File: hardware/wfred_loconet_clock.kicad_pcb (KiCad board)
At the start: 2 copper layers, 124 x 35 mm, 65 parts, among them IC201 ATMEGA328P-A, J301 Molex 95501-6669, K301 TERMINATION, K401 UART_ESP, K402 UART_AVR, P201 ISP, P401 ESP_BOOTLOAD, P501 CLOCK, Q301 BC817-40, Q302 BC817-40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

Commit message: Fixed PCB after untangling
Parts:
- removed C201, C202, C203, C204, C303: 100n, Capacitors_SMD:C_0805_HandSoldering
- removed C205, C206: 22p, Capacitors_SMD:C_0805_HandSoldering
- removed C301: 1n, Capacitors_SMD:C_0805_HandSoldering
- removed C302: 47p, Capacitors_SMD:C_0805_HandSoldering
- removed C304, C305: 22u, Capacitors_SMD:C_0805_HandSoldering
- removed D301, D302, D303: BAR43, TO_SOT_Packages_SMD:SOT-23_Handsoldering
- removed IC201: ATMEGA328P-A, Housings_QFP:TQFP-32_7x7mm_Pitch0.8mm
- removed J301: Molex 95501-6669, myFootprints:Molex_95501-6669
- removed K301: TERMINATION, Pin_Headers:Pin_Header_Straight_1x03_Pitch2.54mm
- removed K402: UART_AVR, Pin_Headers:Pin_Header_Straight_1x03_Pitch2.54mm
- removed P201: ISP, Pin_Headers:Pin_Header_Straight_2x03_Pitch2.54mm
- removed Q301, Q302, Q303: BC817-40, TO_SOT_Packages_SMD:SOT-23_Handsoldering
- removed R201: 10k, Capacitors_SMD:C_0805_HandSoldering
- removed R301: 4k7, Capacitors_SMD:C_0805_HandSoldering
- removed R302, R304, R310: 47k, Capacitors_SMD:C_0805_HandSoldering
- removed R303: 47R, Capacitors_SMD:C_0805_HandSoldering
- removed R305: 2k2, Capacitors_SMD:C_0805_HandSoldering
- removed R306: 82k, Capacitors_SMD:C_0805_HandSoldering
- removed R307, R308: 12R, Capacitors_SMD:C_0805_HandSoldering
- removed R309, R401, R402: 100k, Capacitors_SMD:C_0805_HandSoldering
- removed U301: TC1240, TO_SOT_Packages_SMD:SOT-23-6_Handsoldering
- removed X201: myCRYSTAL, Crystals:Crystal_SMD_TXC_7M-4pin_3.2x2.5mm_HandSoldering
- moved K401 1.54 mm to (76.5, 107.0)
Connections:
- U401 pad 1: VCC -> (no net)
- U401 pad 13: LOCO2 -> CLOCK2
- U401 pad 14: LOCO1 -> CLOCK1
- U401 pad 2: Net-(R401-Pad2) -> (no net)
- U401 pad 4: CLOCK1 -> LOCO1
- U401 pad 5: CLOCK2 -> LOCO2
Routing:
- net GND: track 381.9 -> 56.0 mm, vias 5 -> 0
- net VCC: track 244.7 -> 16.0 mm
- net CLOCK1: track 90.1 -> 0.00 mm, vias 1 -> 0
- net CLOCK2: track 82.9 -> 0.00 mm, vias 1 -> 0
- net THIS_TXD: track 81.0 -> 0.00 mm, vias 1 -> 0
- net THIS_RXD: track 76.3 -> 0.00 mm, vias 1 -> 0
- net Net-(D501-Pad2): track 70.5 -> 0.00 mm
- net MISO: track 68.0 -> 0.00 mm, vias 3 -> 0
- net LOCO2: track 65.1 -> 0.00 mm, vias 1 -> 0
- net LOCO1: track 64.4 -> 0.00 mm, vias 1 -> 0
- net +5V: track 63.1 -> 0.00 mm, vias 1 -> 0
- net ESTOP: track 62.2 -> 0.00 mm, vias 3 -> 0
- net SCK: track 59.9 -> 0.00 mm, vias 3 -> 0
- net +BATT: track 57.1 -> 0.00 mm, vias 2 -> 0
- net RESET: track 51.2 -> 0.00 mm, vias 1 -> 0
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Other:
- board text added: "WiFi-Clock rev0.3 Heiko Rosemann"
- board text removed: "wfred rev0.2 Heiko Rosemann"

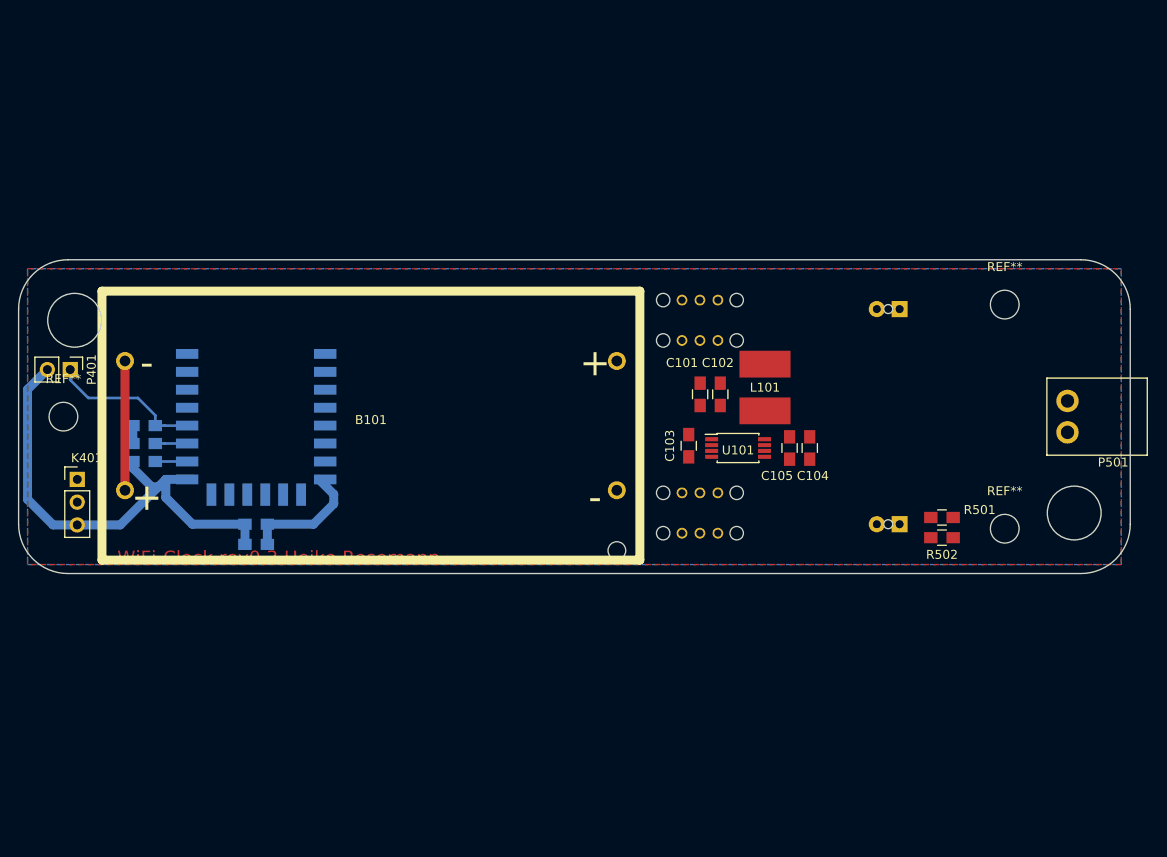
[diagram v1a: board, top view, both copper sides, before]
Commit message: Change clock schematic and PCB
- Remove slide switches, replace with single push button
- Add status LED
- Re-add battery measurement connection

- Change PCB form factor to fit NewAgeEnclosures Compact AA housing
- Re-layout PCB
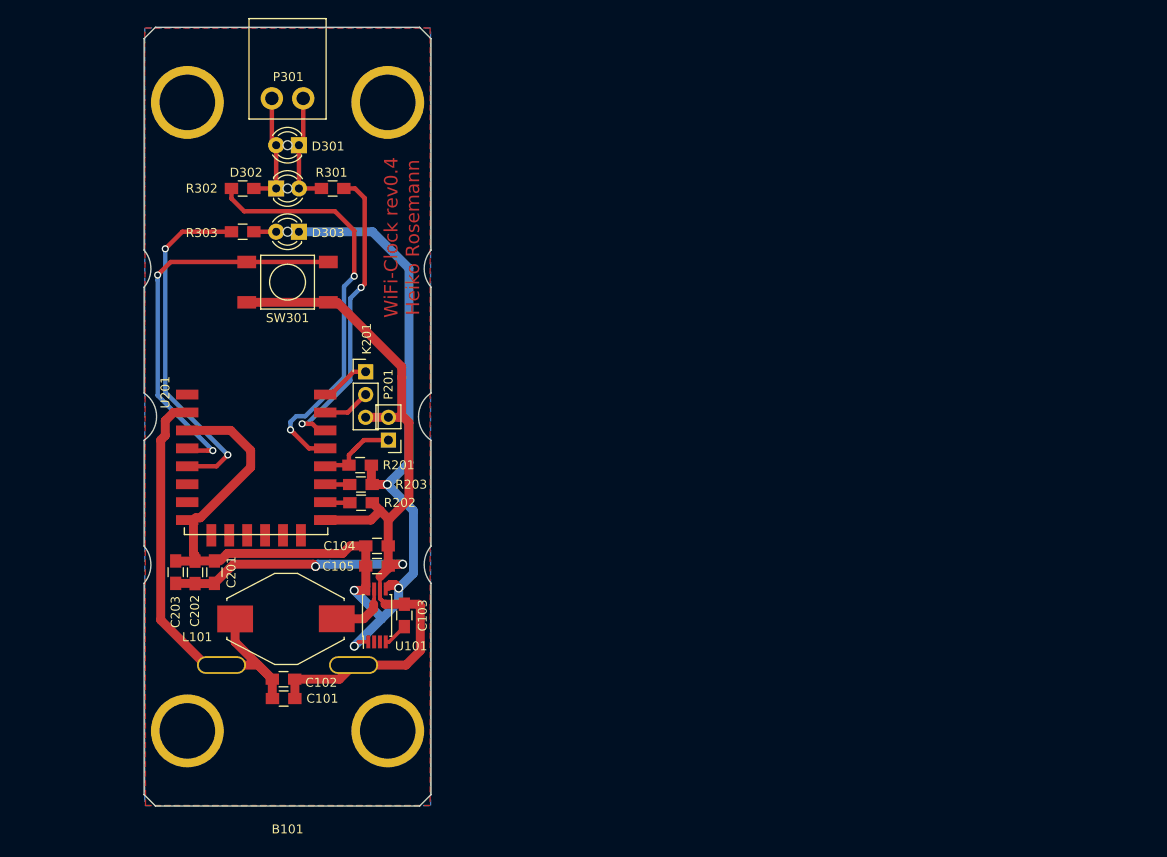
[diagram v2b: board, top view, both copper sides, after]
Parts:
- removed C401: 100n, Capacitors_SMD:C_0805_HandSoldering
- removed C402: 22u, Capacitors_SMD:C_0805_HandSoldering
- removed D501, D502: red, myFootprints:LED_D3.0mm
- removed K401: UART_ESP, Pin_Headers:Pin_Header_Straight_1x03_Pitch2.54mm
- removed P401: ESP_BOOTLOAD, Pin_Headers:Pin_Header_Straight_1x02_Pitch2.54mm
- removed P501: CLOCK, myFootprints:AKL183-02
- removed R403, R404, R405: 10k, Capacitors_SMD:C_0805_HandSoldering
- removed R501, R502: 220, Capacitors_SMD:C_0805_HandSoldering
- removed REF** (x3): MountingHole_3.2mm_M3, Mounting_Holes:MountingHole_3.2mm_M3
- removed SW501, SW502, SW503, SW504: SWITCH_INV, myFootprints:OS102011MS2Q
- removed U401: ESP-12E, ESP8266:ESP-12E_SMD
- added C201: 100n, Capacitors_SMD:C_0805_HandSoldering, F.Cu at (91.8, 117.3)
- added C202: 22u, Capacitors_SMD:C_0805_HandSoldering, F.Cu at (89.7, 117.4)
- added C203: 100u, Capacitors_SMD:C_0805_HandSoldering, F.Cu at (87.5, 117.3)
- added D301: red, myFootprints:LED_D3.0mm, F.Cu at (101.3, 69.7)
- added D302: red, myFootprints:LED_D3.0mm, F.Cu at (98.7, 74.5)
- added D303: red, myFootprints:LED_D3.0mm, F.Cu at (101.3, 79.4)
- added K201: UART_ESP, Pin_Headers:Pin_Header_Straight_1x03_Pitch2.54mm, F.Cu at (108.7, 95.0)
- added P201: ESP_BOOTLOAD, Pin_Headers:Pin_Header_Straight_1x02_Pitch2.54mm, F.Cu at (111.3, 102.6)
- added P301: CLOCK, myFootprints:AKL183-02, F.Cu at (101.8, 64.5)
- added R201: 10k, Capacitors_SMD:C_0805_HandSoldering, F.Cu at (108.1, 105.4)
- added R202: 10k, Capacitors_SMD:C_0805_HandSoldering, F.Cu at (108.2, 109.6)
- added R203: 10k, Capacitors_SMD:C_0805_HandSoldering, F.Cu at (108.2, 107.6)
- added R301: 220, Capacitors_SMD:C_0805_HandSoldering, F.Cu at (105.0, 74.5)
- added R302: 220, Capacitors_SMD:C_0805_HandSoldering, F.Cu at (95.0, 74.5)
- added R303: 330, Capacitors_SMD:C_0805_HandSoldering, F.Cu at (95.0, 79.4)
- added SW301: SW_PUSH, myFootprints:Taster_9319, F.Cu at (100.0, 85.0)
- added U201: ESP-12E, ESP8266:ESP-12E_SMD, F.Cu at (89.5, 97.5)
- B101: value BATT_HOLDER -> BATT_HOLDER_2; footprint myFootprints:KEYSTONE1013 -> myFootprints:NEW_AGE_COMPACT_AA_PCBEdges
- L101: footprint myFootprints:L_2424_HandSoldering -> Inductors_SMD:L_Fastron_PISN_Handsoldering
- moved L101 59.3 mm to (99.8, 122.6), turned to 180 degrees
- moved C102 58.2 mm to (99.5, 129.3), turned to 0 degrees
- moved C101 57.5 mm to (99.6, 131.4), turned to 0 degrees
- moved C104 49.5 mm to (110.0, 114.4), turned to 0 degrees
- moved C105 47.9 mm to (110.0, 116.7), turned to 0 degrees
- moved U101 44.4 mm to (110.0, 122.2), turned to 90 degrees
- moved C103 36.9 mm to (113.0, 122.2)
- moved B101 9.35 mm to (100.0, 100.0)
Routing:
- net VCC: track 16.0 -> 139.7 mm, vias 0 -> 4
- net GND: track 56.0 -> 119.2 mm, vias 0 -> 2
- net +BATT: track 0.00 -> 51.7 mm
- net CLOCK2: track 0.00 -> 46.1 mm, vias 0 -> 2
- net KEY: track 0.00 -> 44.0 mm, vias 0 -> 2
- net STATUS_LED: track 0.00 -> 38.4 mm, vias 0 -> 2
- net CLOCK1: track 0.00 -> 33.4 mm, vias 0 -> 2
- net Net-(P401-Pad1): track 17.7 -> 0.00 mm
- net Net-(B101-PadMI1): track 14.4 -> 0.00 mm
- net Net-(D301-Pad2): track 0.00 -> 12.8 mm
- net Net-(D301-Pad1): track 0.00 -> 12.8 mm
- net Net-(P201-Pad1): track 0.00 -> 10.3 mm
- net Net-(L101-Pad2): track 0.00 -> 7.34 mm
- net Net-(K201-Pad1): track 0.00 -> 6.45 mm
- net Net-(K201-Pad2): track 0.00 -> 6.04 mm
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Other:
- board size 124 x 35 mm -> 32 x 86.9 mm
- net class Default: trace_width 0.3 -> 0.5
- board text added: "WiFi-Clock rev0.4 Heiko Rosemann"
- board text removed: "WiFi-Clock rev0.3 Heiko Rosemann"

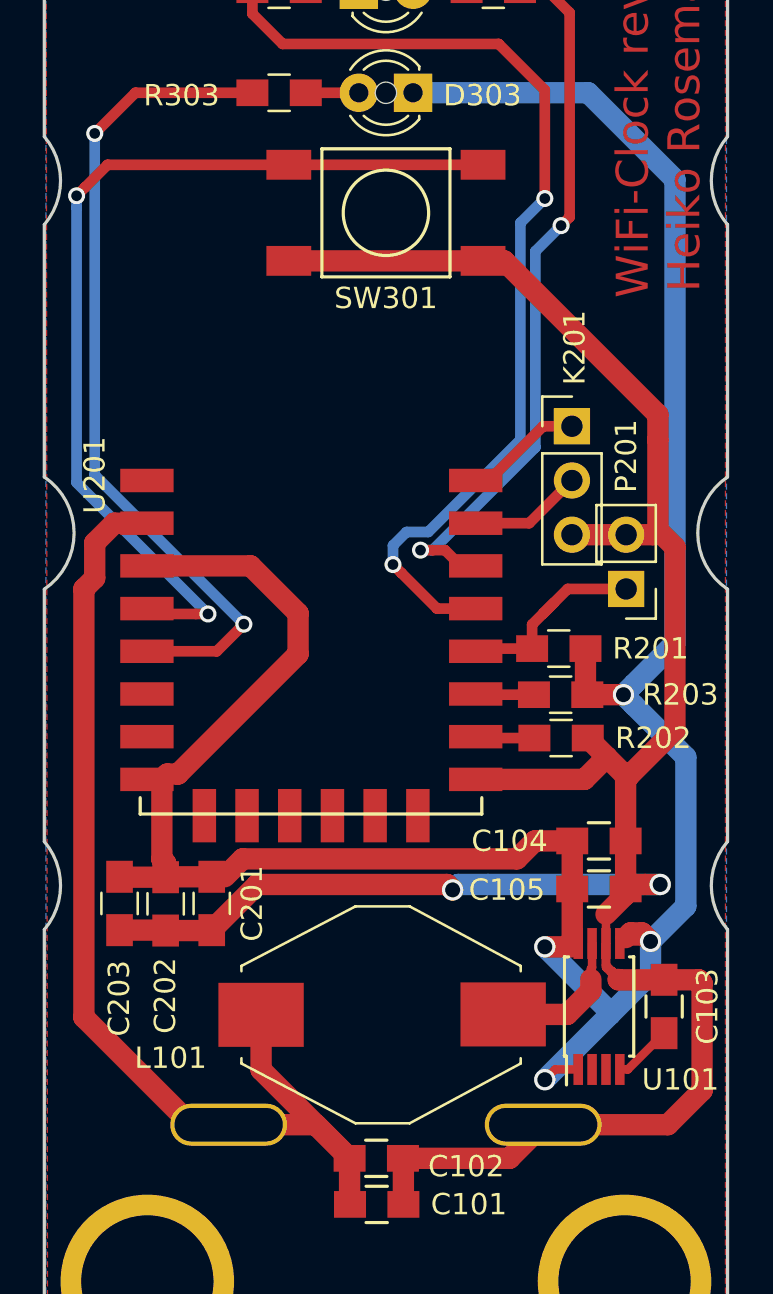
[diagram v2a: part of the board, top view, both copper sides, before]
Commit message: Changed PCB and code to closer match first PCB
- Add battery measurement resistors
- Move key, status LED and clock I/O-pins around to match first PCB
  (except for CLOCK1 which is on low power pin in first version)
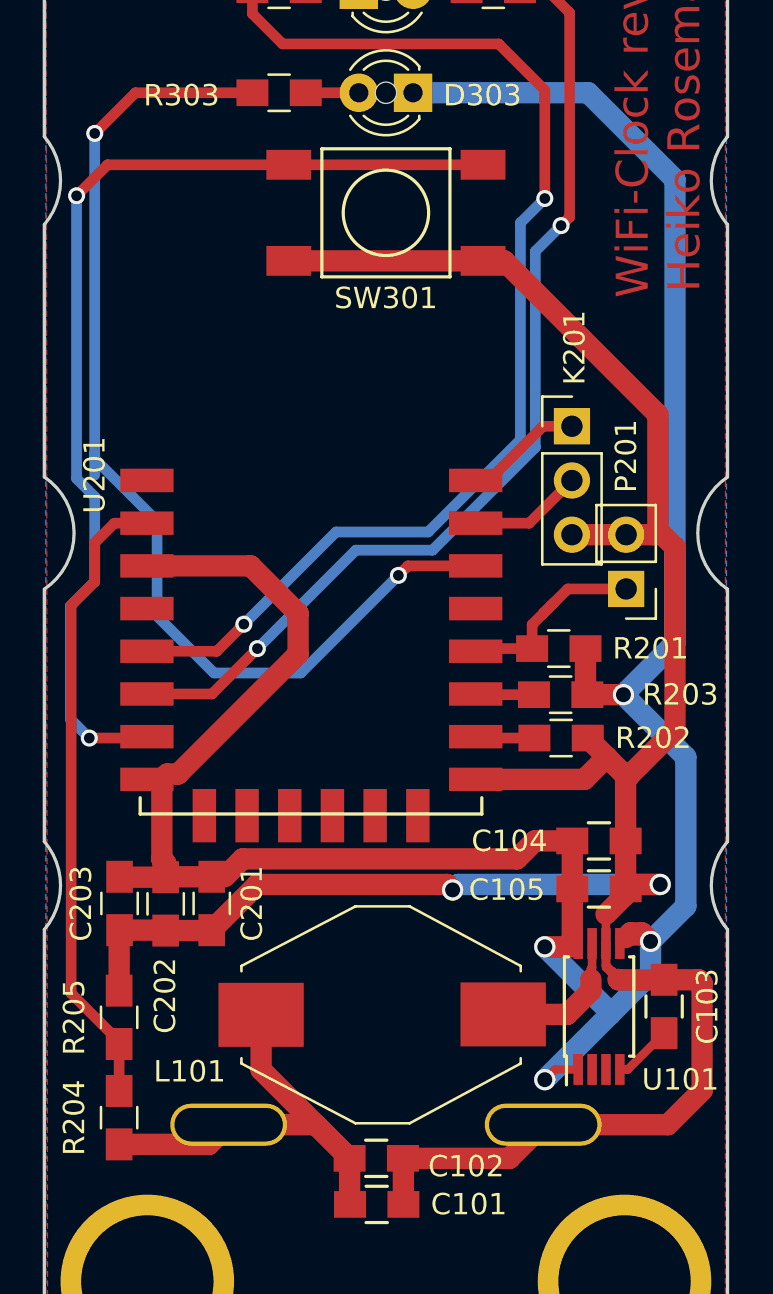
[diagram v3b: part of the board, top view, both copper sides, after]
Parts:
- added R204: 100k, Capacitors_SMD:C_0805_HandSoldering, F.Cu at (87.5, 127.4)
- added R205: 47k, Capacitors_SMD:C_0805_HandSoldering, F.Cu at (87.5, 122.7)
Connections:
- U201 pad 13: CLOCK2 -> (no net)
- U201 pad 14: CLOCK1 -> STATUS_LED
- U201 pad 2: +BATT -> Net-(R204-Pad2)
- U201 pad 4: KEY -> (no net)
- U201 pad 5: STATUS_LED -> CLOCK2
- U201 pad 6: (no net) -> CLOCK1
- U201 pad 7: (no net) -> KEY
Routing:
- net Net-(R204-Pad2): track 0.00 -> 30.6 mm
- net +BATT: track 51.7 -> 24.2 mm
- net CLOCK1: track 33.4 -> 46.1 mm
- net STATUS_LED: track 38.4 -> 50.4 mm
- net CLOCK2: track 46.1 -> 54.1 mm
- net KEY: track 44.0 -> 49.7 mm
- net GND: track 119.2 -> 122.1 mm

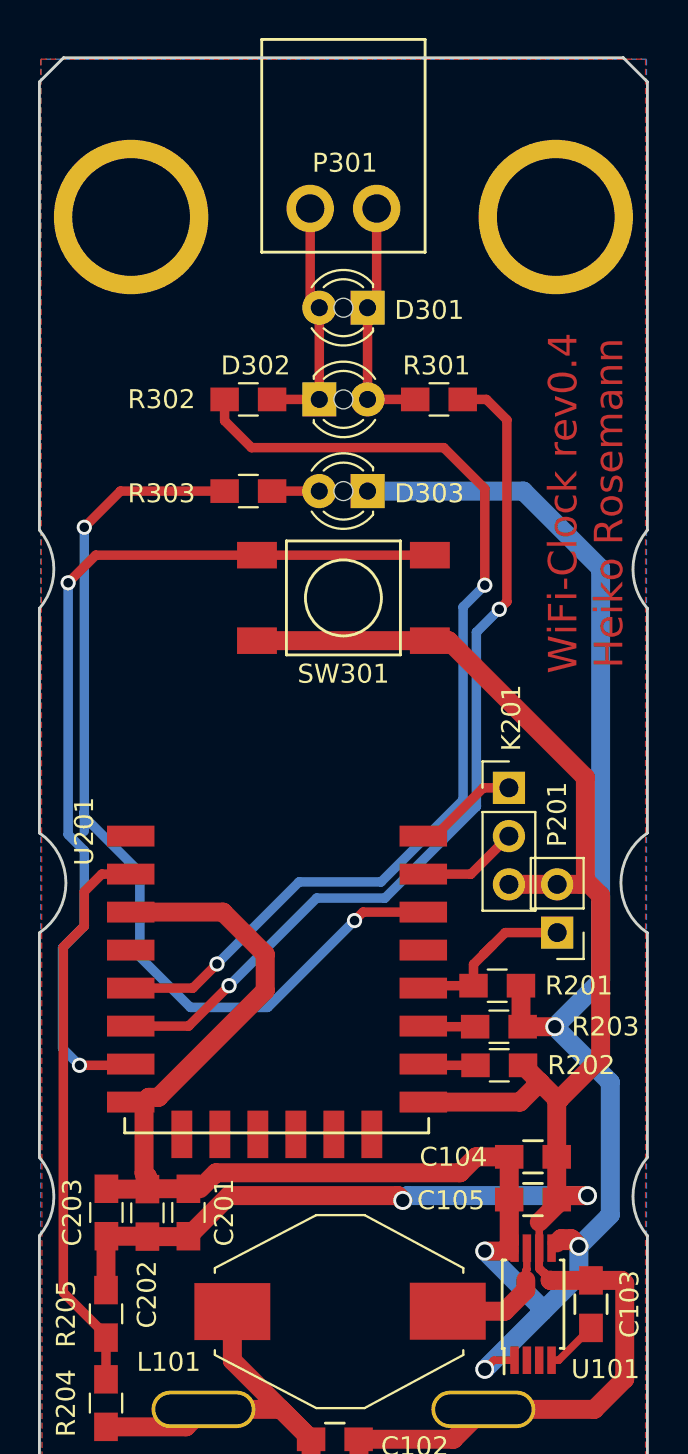
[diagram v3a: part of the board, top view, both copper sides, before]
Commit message: Added more keys to the PCB for adjusting the time
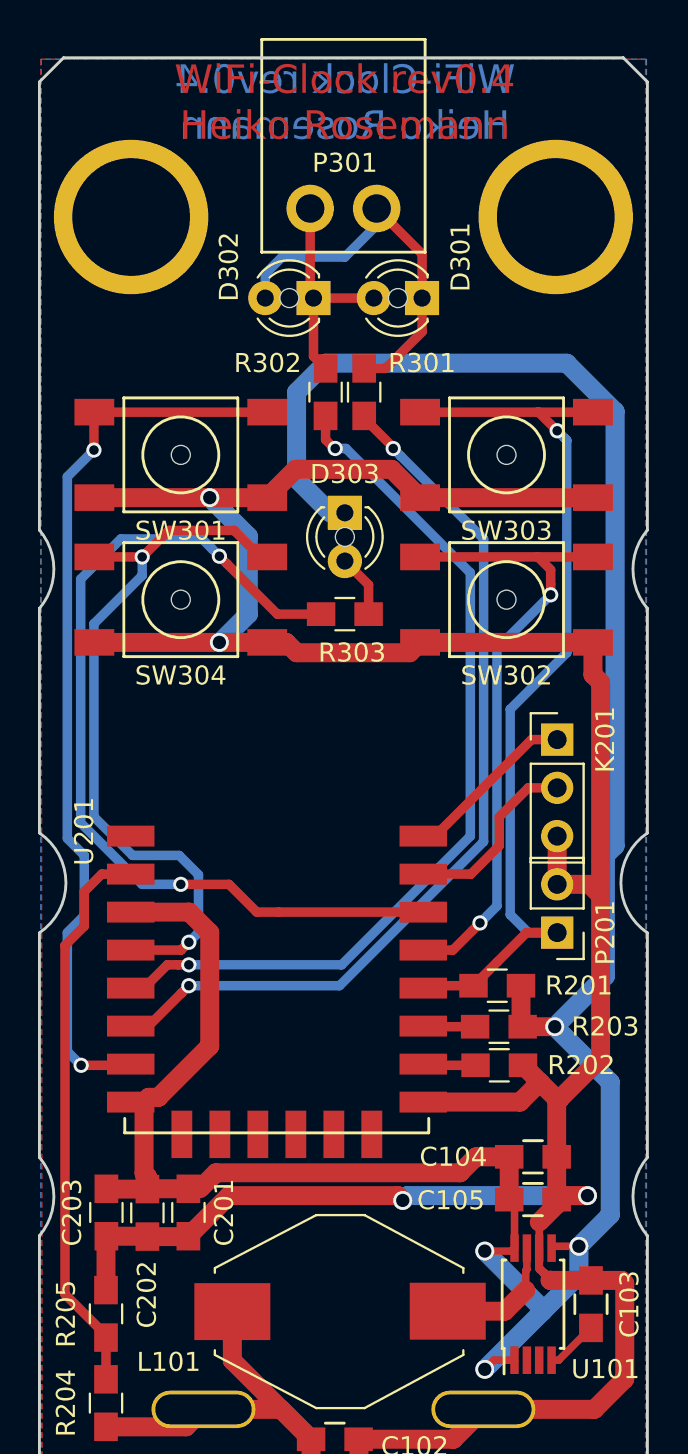
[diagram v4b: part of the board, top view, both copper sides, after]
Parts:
- added SW302: SW_PUSH, myFootprints:Taster_9319, F.Cu at (108.6, 85.1)
- added SW303: SW_PUSH, myFootprints:Taster_9319, F.Cu at (108.6, 77.5)
- added SW304: SW_PUSH, myFootprints:Taster_9319, F.Cu at (91.4, 85.1)
- moved SW301 11.4 mm to (91.4, 77.5)
- moved R303 8.23 mm to (100.1, 85.9)
- moved D302 5.34 mm to (98.4, 69.2), turned to 180 degrees
- moved R302 4.08 mm to (99.1, 74.2), turned to 270 degrees
- moved R301 3.96 mm to (101.1, 74.2), turned to 270 degrees
- moved K201 3.59 mm to (111.3, 92.5)
- moved D301 2.91 mm to (104.1, 69.2)
- moved D303 1.65 mm to (100.1, 80.5), turned to 270 degrees
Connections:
- net Net-(P201-Pad1) renamed KEY_MINUTE
- SW301 pad 2: KEY -> KEY_CONF
- U201 pad 13: (no net) -> KEY_HOUR
- U201 pad 4: (no net) -> KEY
- U201 pad 7: KEY -> KEY_CONF
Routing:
- net GND: track 122.1 -> 173.0 mm, vias 2 -> 4
- net KEY_CONF: track 0.00 -> 48.4 mm, vias 0 -> 2
- net KEY_MINUTE: track 10.3 -> 49.3 mm, vias 0 -> 1
- net KEY_HOUR: track 0.00 -> 34.5 mm, vias 0 -> 2
- net VCC: track 139.7 -> 152.1 mm
- net KEY: track 49.7 -> 38.1 mm
- net CLOCK2: track 54.1 -> 46.1 mm
- net Net-(D301-Pad1): track 12.8 -> 20.4 mm
- net Net-(K201-Pad2): track 6.04 -> 10.5 mm
- net Net-(K201-Pad1): track 6.45 -> 10.0 mm
- net STATUS_LED: track 50.4 -> 47.3 mm
- net Net-(D301-Pad2): track 12.8 -> 11.9 mm
- net CLOCK1: track 46.1 -> 46.9 mm
- net Net-(D303-Pad2): track 2.48 -> 3.31 mm
- net Net-(L101-Pad2): track 7.34 -> 6.80 mm
